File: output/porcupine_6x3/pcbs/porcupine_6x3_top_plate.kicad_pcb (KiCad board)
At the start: 2 copper layers, 166.2 x 113.7 mm, 0 parts

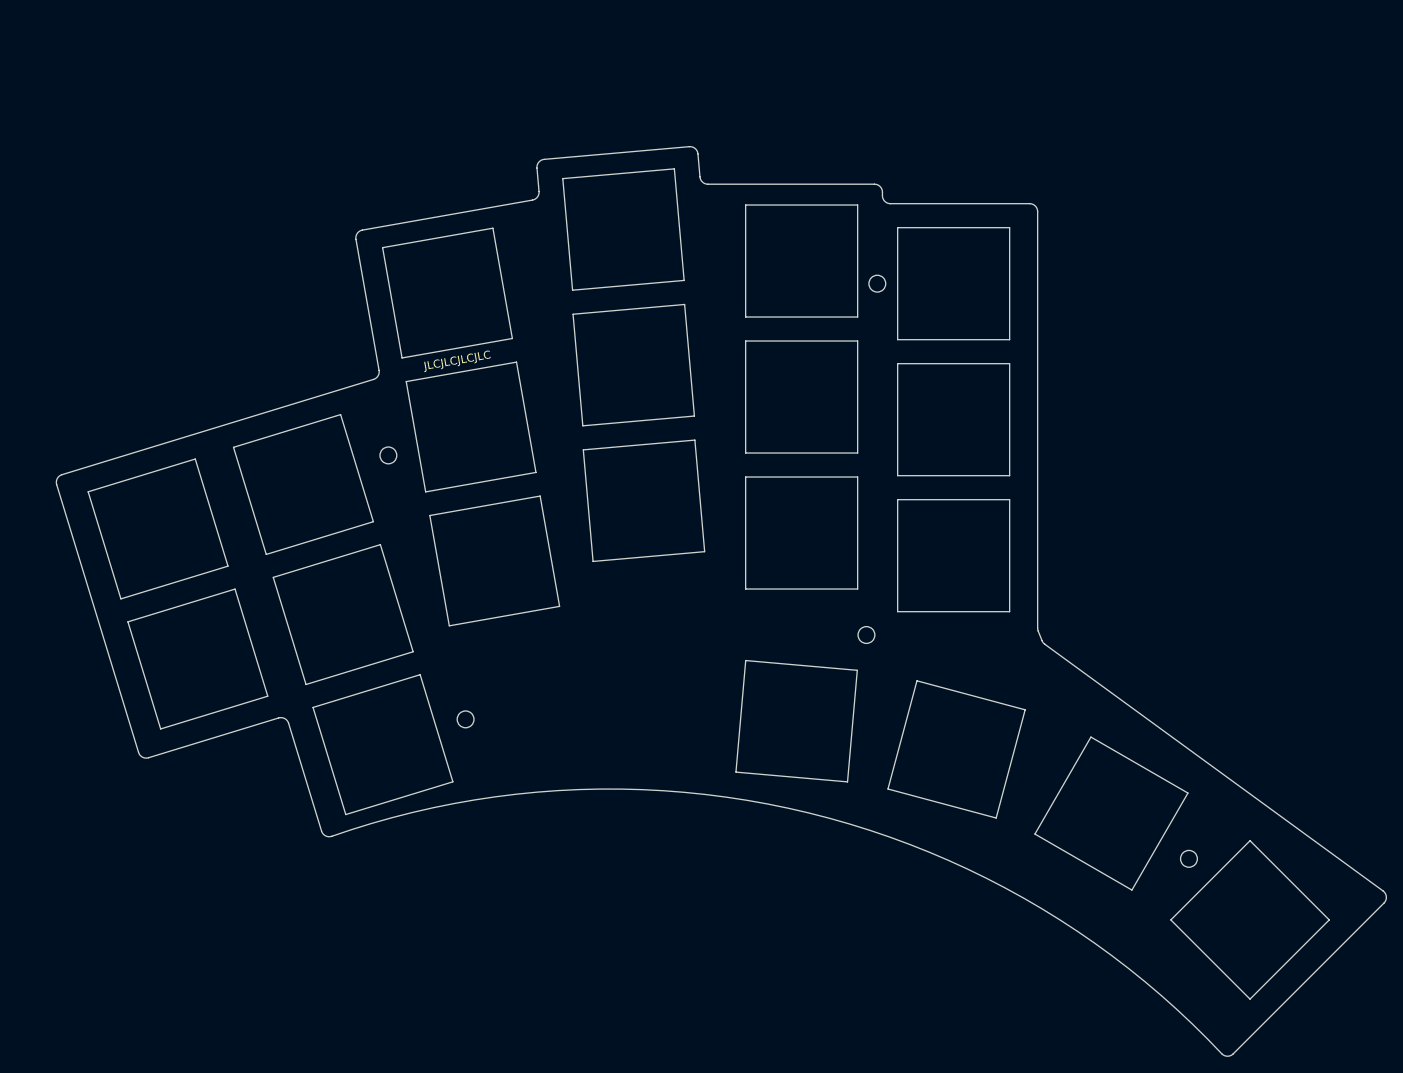
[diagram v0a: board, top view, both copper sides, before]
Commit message: Update 6x3 variant
* Removed unnecessary P19 via
* Fix outer column stagger
* Fix P19 matrix ring bottom via
* Resized GND zones
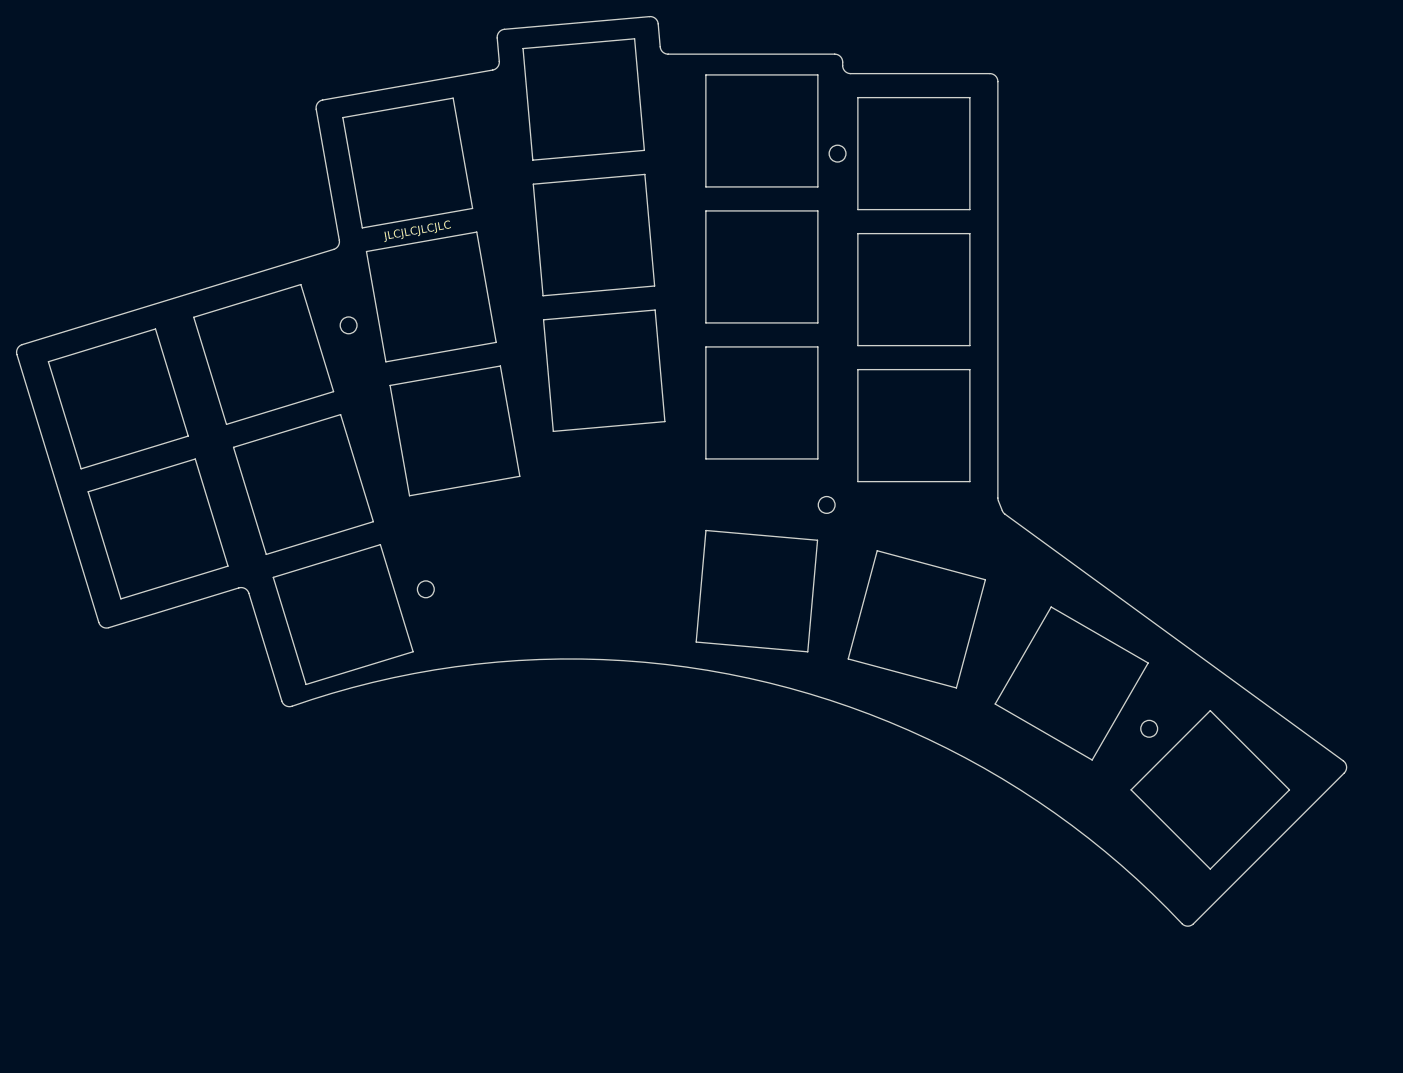
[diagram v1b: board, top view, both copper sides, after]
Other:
- outline, holes or cut-outs redrawn
